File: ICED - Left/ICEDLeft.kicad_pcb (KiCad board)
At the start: 2 copper layers, 176.2 x 145.8 mm, 165 parts, among them P1 Conn_ARM_JTAG_SWD_10, P2 DX07S024XJ1R1100, P3 CONN_17, P4 692121130100, P5 RGB Out, Q1 TC1264, U1 MK20DX256VLH7, U2 IS31FL3737-QFLS4-TR, X1 NX3225SA-16.000MHZ-STD-CSR-

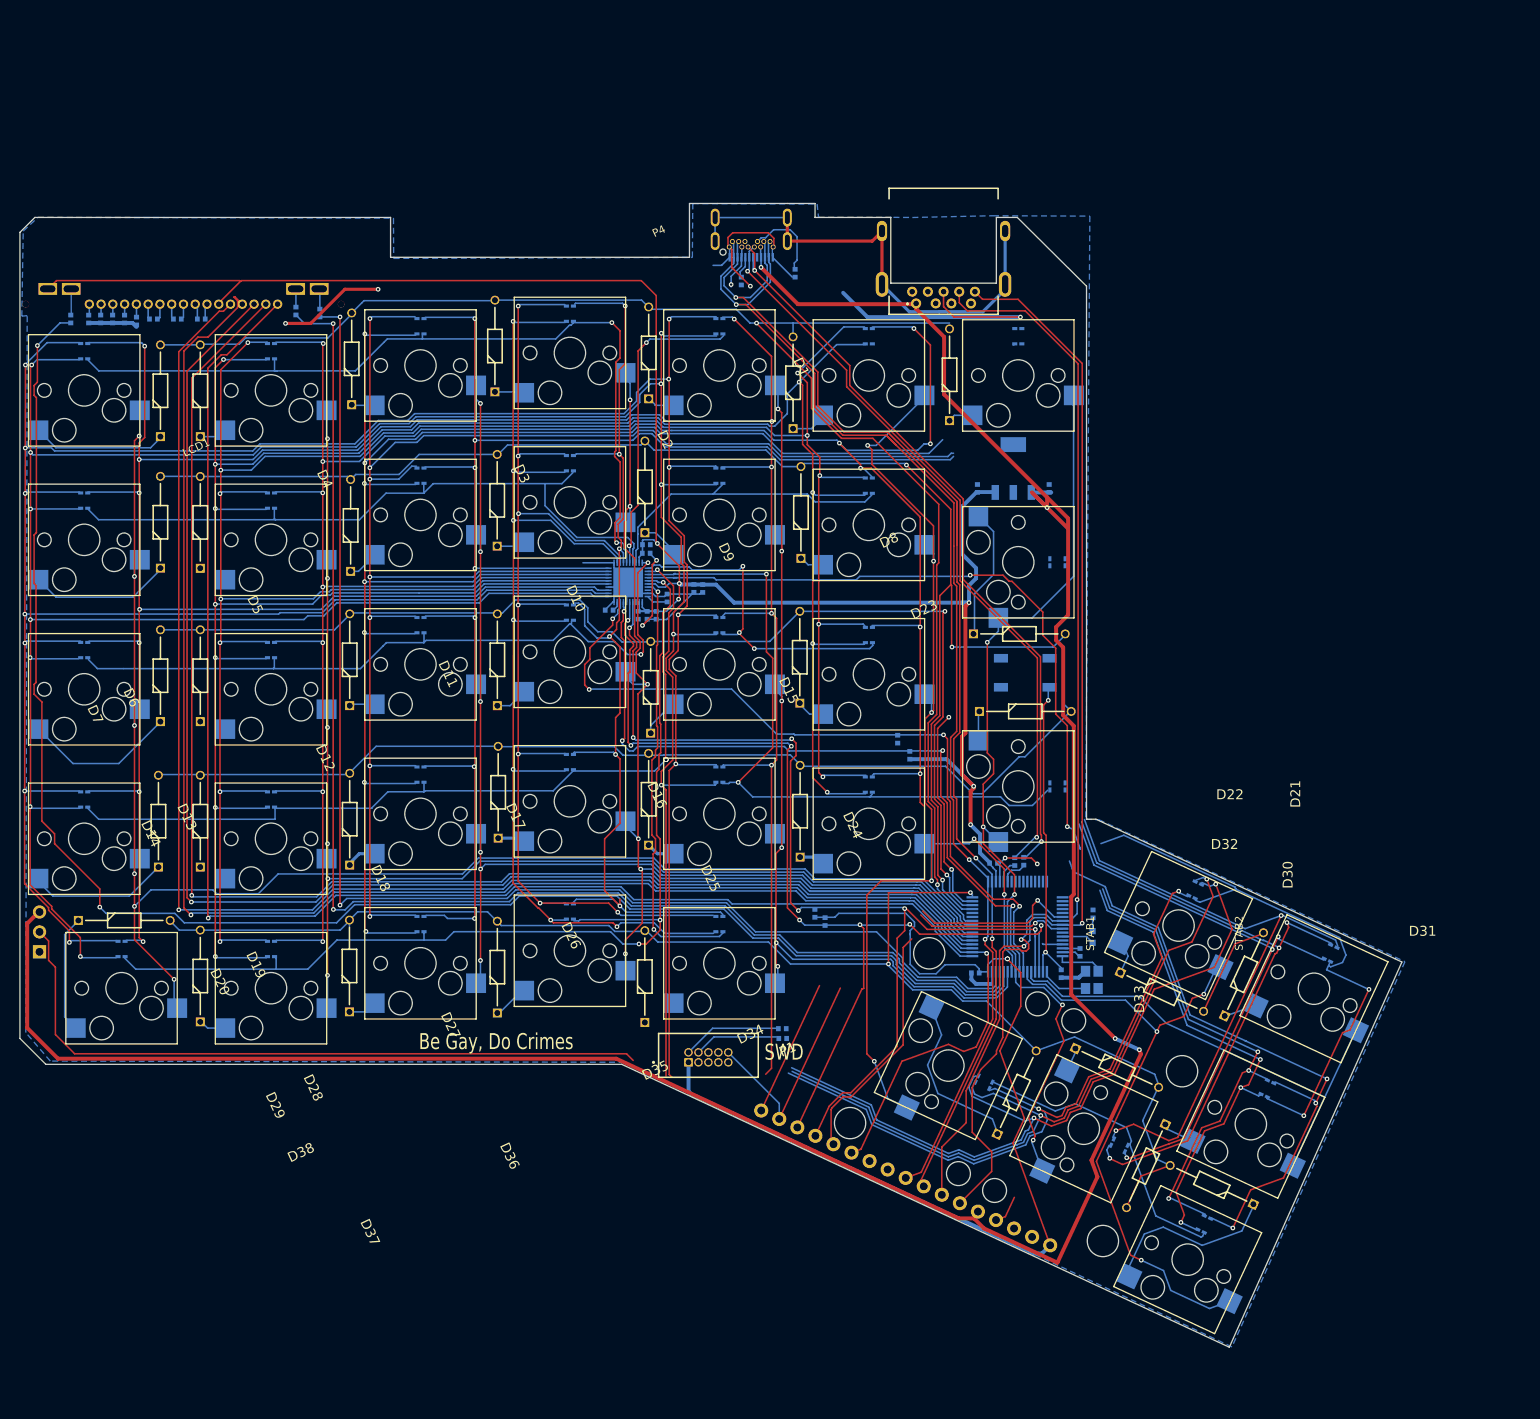
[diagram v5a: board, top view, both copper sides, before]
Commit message: Migrate schematics and more routing
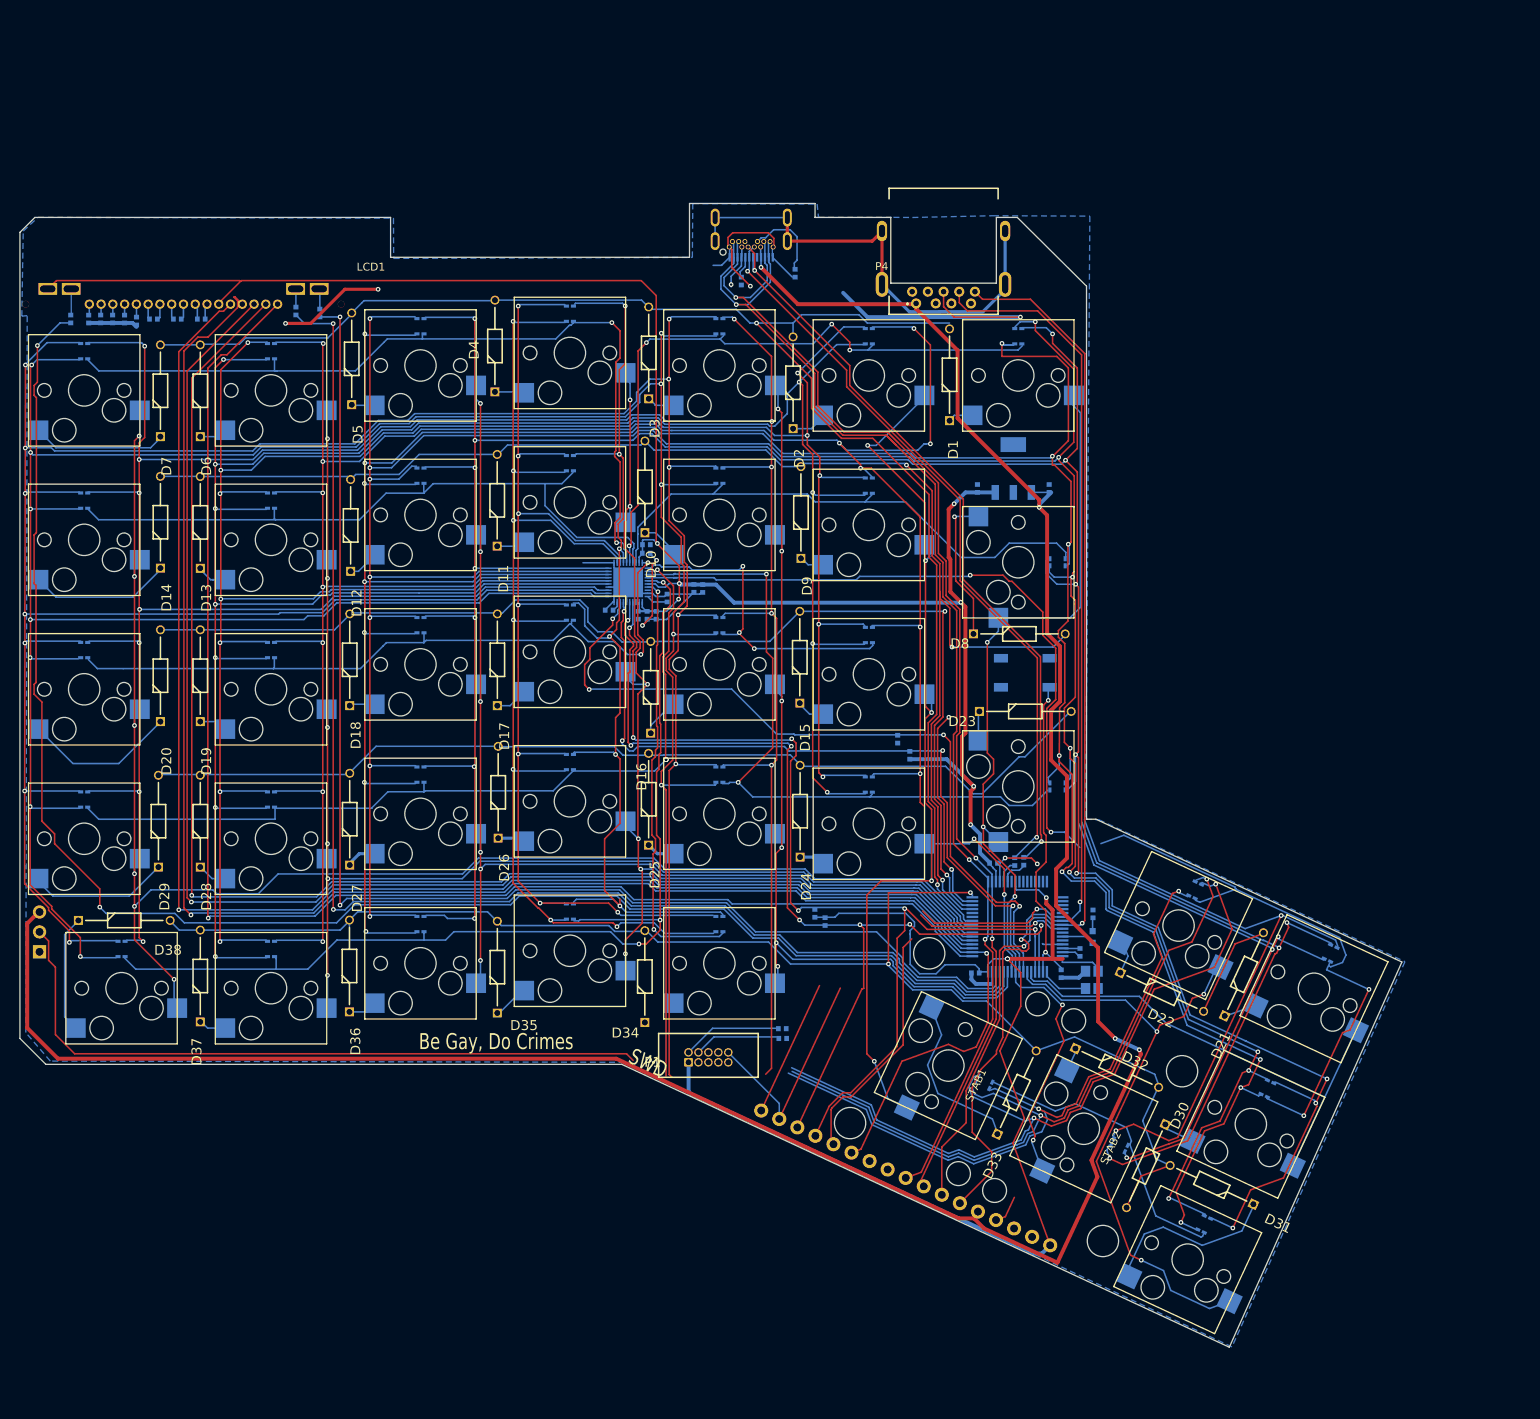
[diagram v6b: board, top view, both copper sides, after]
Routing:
- net /mcu/ledmatrix_2/Red3: track 280.6 -> 390.5 mm, vias 10 -> 15
- net /mcu/ledmatrix_2/Green3: track 276.9 -> 383.3 mm, vias 10 -> 15
- net /mcu/ledmatrix_2/Blue3: track 267.4 -> 368.4 mm, vias 10 -> 15
- net /mcu/ledmatrix_2/Row1B: track 39.2 -> 82.3 mm, vias 2 -> 4
- net /mcu/ledmatrix_2/Row2B: track 38.7 -> 69.0 mm
- net VDD: track 381.6 -> 400.5 mm, vias 8 -> 10
- net +5V: track 338.4 -> 328.3 mm
- net /mcu/RX1: track 158.8 -> 152.9 mm
- net Net-(D13-Pad1): track 0.00 -> 5.40 mm
- net Net-(D19-Pad1): track 0.00 -> 4.18 mm
- net Net-(D28-Pad1): track 0.00 -> 3.89 mm
- net /Col3: track 119.4 -> 123.0 mm
- net Net-(D8-Pad1): track 16.8 -> 19.0 mm, vias 0 -> 1
- net /mcu/ledmatrix_2/Row4C: track 160.5 -> 162.0 mm
- net Net-(R6-Pad1): track 21.5 -> 20.0 mm
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
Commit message: mostly routed
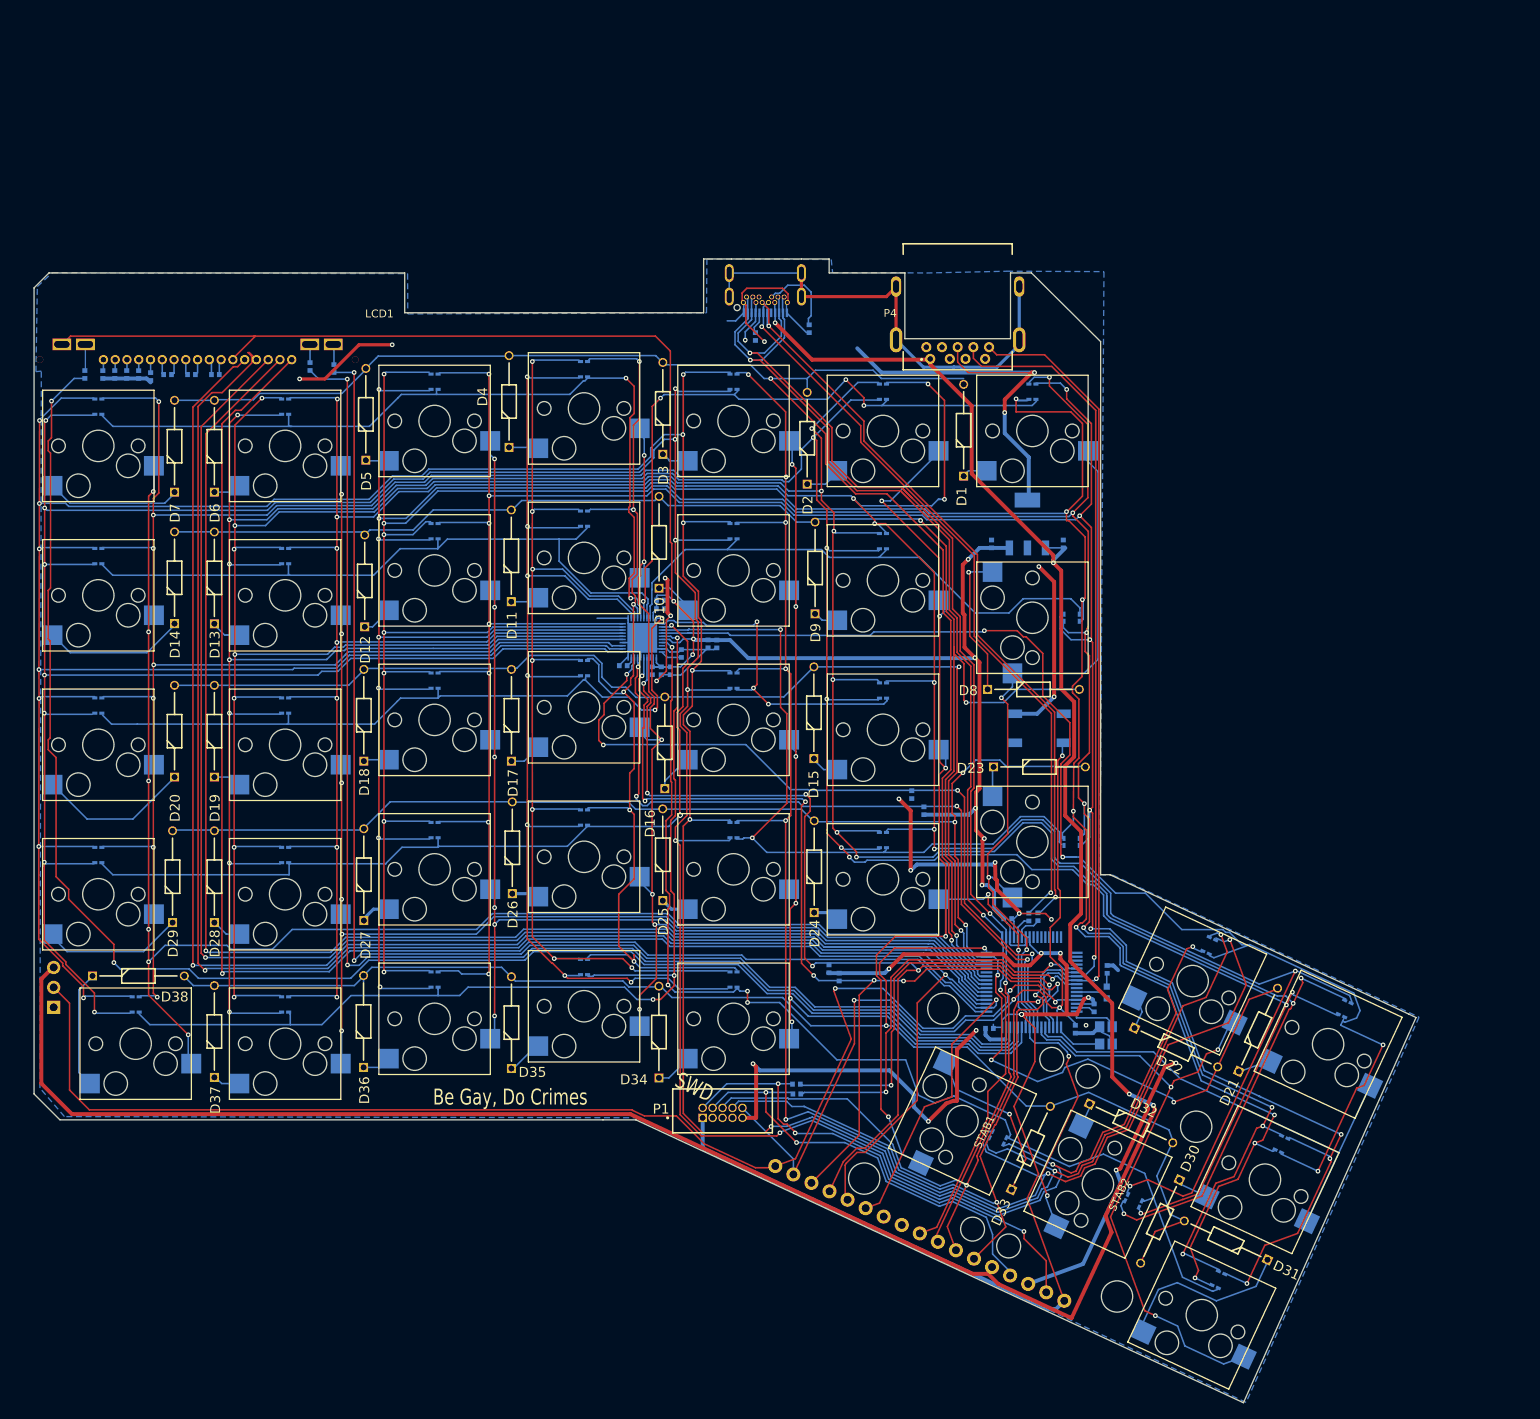
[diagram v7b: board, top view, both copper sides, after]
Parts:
- moved C12 7.30 mm to (24.8, 79.2)
- moved D1 7.30 mm to (126.3, 92.1)
- moved D24 7.30 mm to (107.2, 147.8)
- moved D27 7.30 mm to (49.8, 148.8)
- moved LED35 7.30 mm to (77.9, 154.7)
- moved LED36 7.30 mm to (58.8, 156.3)
- moved S27 7.30 mm to (58.8, 142.2)
- moved P2 7.30 mm to (97.4, 70.6)
- moved D32 7.30 mm to (142.3, 172.2)
- moved D15 7.30 mm to (107.2, 128.1)
- moved S31 7.30 mm to (156.6, 199.1)
- moved D8 7.30 mm to (129.3, 119.3)
- moved LED9 7.30 mm to (116.0, 100.4)
- moved R4 7.30 mm to (119.6, 132.7)
- moved D29 7.30 mm to (25.4, 149.0)
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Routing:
- net VSS: track 137.1 -> 305.2 mm, vias 8 -> 21
- net /mcu/RGBOUT: track 109.1 -> 170.5 mm, vias 0 -> 3
- net /mcu/SWD_DIO: track 12.7 -> 63.0 mm, vias 0 -> 3
- net /mcu/ledmatrix_2/Row5B: track 92.3 -> 139.7 mm, vias 2 -> 4
- net /mcu/ledmatrix_2/Green2: track 395.0 -> 439.0 mm, vias 15 -> 16
- net /Row4: track 164.3 -> 207.6 mm, vias 2 -> 6
- net /mcu/SWD_CLK: track 14.7 -> 55.2 mm, vias 0 -> 2
- net /mcu/RX0: track 142.8 -> 180.3 mm, vias 2 -> 3
- net /mcu/MCU_RESET: track 70.1 -> 107.2 mm, vias 2 -> 4
- net /mcu/TX0: track 137.5 -> 174.2 mm, vias 2 -> 3
- net /mcu/ledmatrix_2/Red2: track 397.7 -> 432.4 mm, vias 14 -> 15
- net Net-(R7-Pad1): track 19.4 -> 53.1 mm, vias 1 -> 2
- net Net-(R6-Pad1): track 20.0 -> 51.8 mm, vias 1 -> 2
- net /mcu/ledmatrix_2/Blue2: track 391.5 -> 417.1 mm, vias 15 -> 16
- net /mcu/ledmatrix_2/Red1: track 480.8 -> 496.6 mm, vias 14 -> 15
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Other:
- board text removed: "RX2"
- board text removed: "TX2"

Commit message: Second Revision Finalised
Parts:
- moved R14 32.2 mm to (113.1, 45.1)
- moved LED32 31.9 mm to (161.3, 155.5)
- moved D12 31.9 mm to (63.3, 82.4)
- moved R8 31.9 mm to (96.3, 87.3)
- moved R2 31.9 mm to (149.1, 119.3)
- moved D34 31.9 mm to (100.8, 139.9)
- moved D32 31.9 mm to (155.7, 143.2)
- moved S36 31.9 mm to (72.2, 132.3)
- moved D22 31.9 mm to (161.5, 133.5)
- moved D36 31.9 mm to (63.2, 138.5)
- moved S30 31.9 mm to (178.1, 152.8)
- moved S32 31.9 mm to (156.8, 153.4)
- moved STAB2 31.9 mm to (156.8, 153.4)
- moved C1 31.9 mm to (152.4, 71.8)
- moved LED2 31.9 mm to (129.4, 52.4)
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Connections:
- P3 pad 10: /mcu/RX2 -> (no net)
- P3 pad 11: /mcu/TX2 -> (no net)
- U1 pad 59: /mcu/RX2 -> (no net)
- U1 pad 60: /mcu/TX2 -> (no net)
- U2 pad 28: (no net) -> unconnected-(U2-Pad28)
- U2 pad 33: (no net) -> unconnected-(U2-Pad33)
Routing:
- net VSS: track 305.2 -> 508.6 mm, vias 21 -> 41
- net +5V: track 328.3 -> 336.1 mm, vias 5 -> 4
- net /mcu/D+: track 94.9 -> 99.0 mm
- net /mcu/D-: track 96.1 -> 100.2 mm
- net /Row5: track 181.6 -> 185.7 mm
- net /mcu/RGBOUT: track 170.5 -> 168.5 mm
- net VDD: track 410.5 -> 409.0 mm
- net /mcu/ledmatrix_2/Green1: track 502.9 -> 502.1 mm
- net /mcu/RX1: track 153.1 -> 153.8 mm
- net /mcu/SWD_DIO: track 63.0 -> 62.3 mm
- net /mcu/ledmatrix_2/Blue1: track 467.2 -> 466.6 mm
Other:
- rule pad_to_mask_clearance: 0.0508 -> 0
- board text added: "${revision}"
